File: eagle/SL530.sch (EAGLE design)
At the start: 42 parts, among them IC4 74LVC1G17DBV, IC5 74LVC1G17DBV, U1 LM1117, X1 MC68000

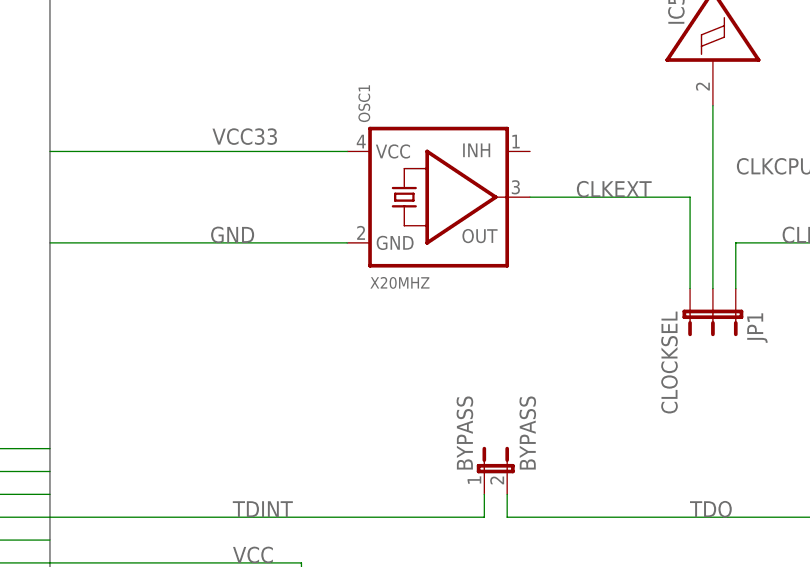
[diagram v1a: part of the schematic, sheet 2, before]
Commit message: Added solder thieves
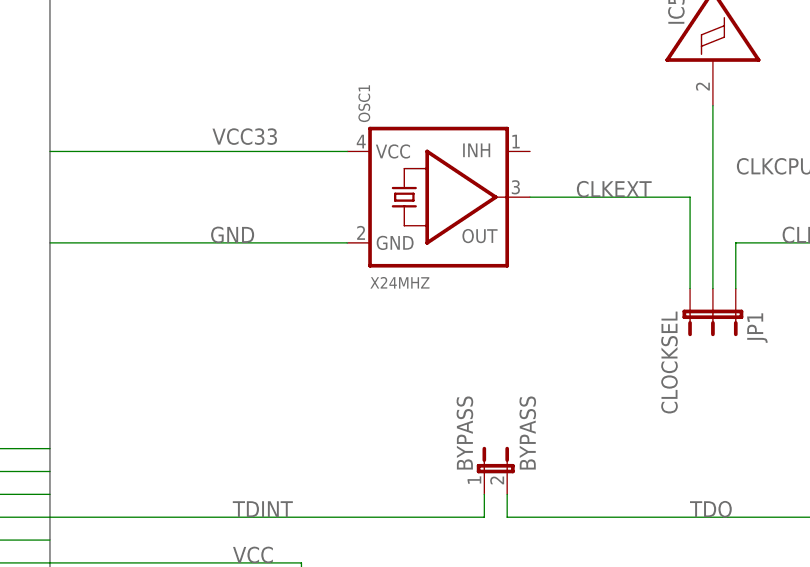
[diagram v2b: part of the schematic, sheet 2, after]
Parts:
- OSC1: value X20MHZ -> X24MHZ
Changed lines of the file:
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@@
 <parts>
 <part name="X1" library="terriblefire" deviceset="MC68000P" device="" value="MC68000"/>
-<part name="OSC1" library="microbuilder" deviceset="OSCILLATOR" device="" value="X20MHZ"/>
+<part name="OSC1" library="microbuilder" deviceset="OSCILLATOR" device="" value="X24MHZ"/>
 <part name="JP1" library="SparkFun-Retired" deviceset="JUMPER-3" device="PTH" value="CLOCKSEL"/>
 <part name="JTAG" library="microbuilder" deviceset="HEADER-1X6" device="ROUND" value="JTAG"/>
